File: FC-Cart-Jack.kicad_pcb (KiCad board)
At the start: 2 copper layers, 98 x 56.8 mm, 6 parts, among them J1 ToCartridge, J2 ToConsole, J3 AudioJack3_SwitchTR, U1 LM321

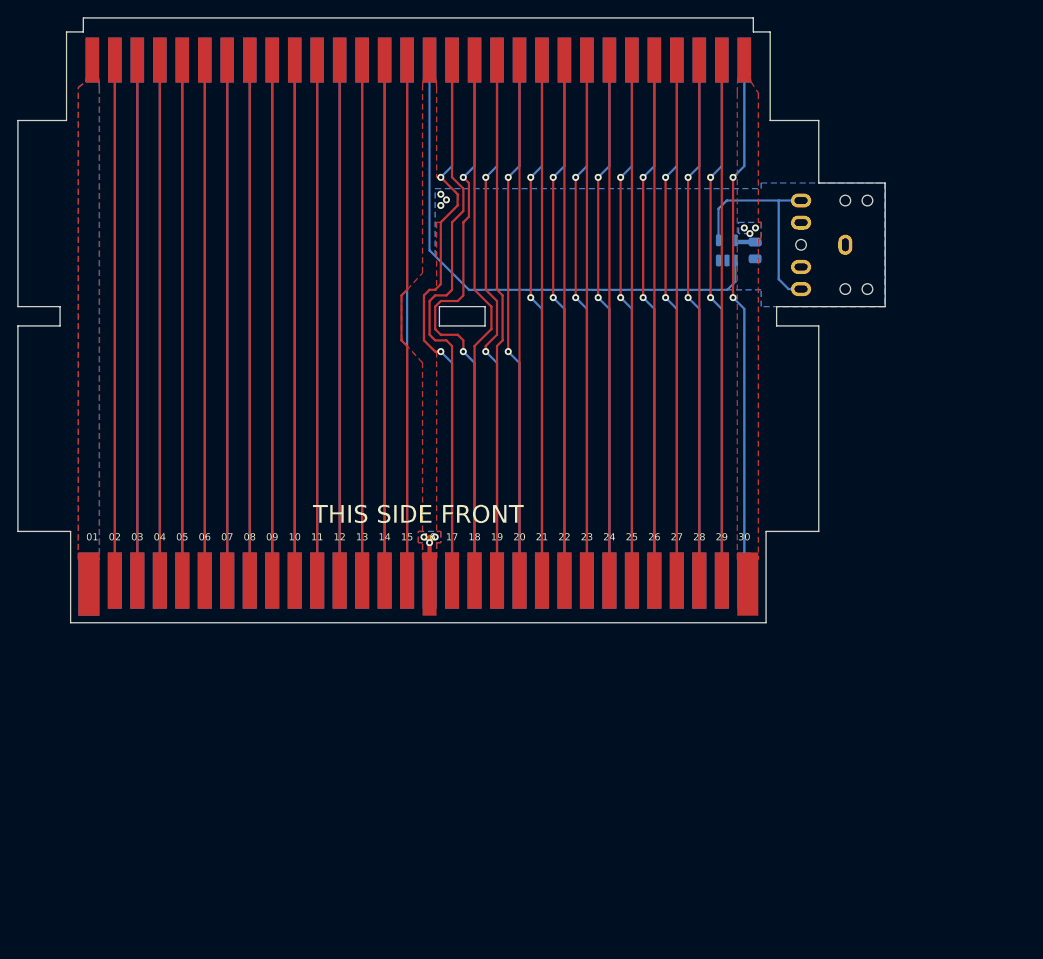
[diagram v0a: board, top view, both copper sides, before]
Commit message: Add silkscreen art
Dagga illustration by @Lockster-Inc
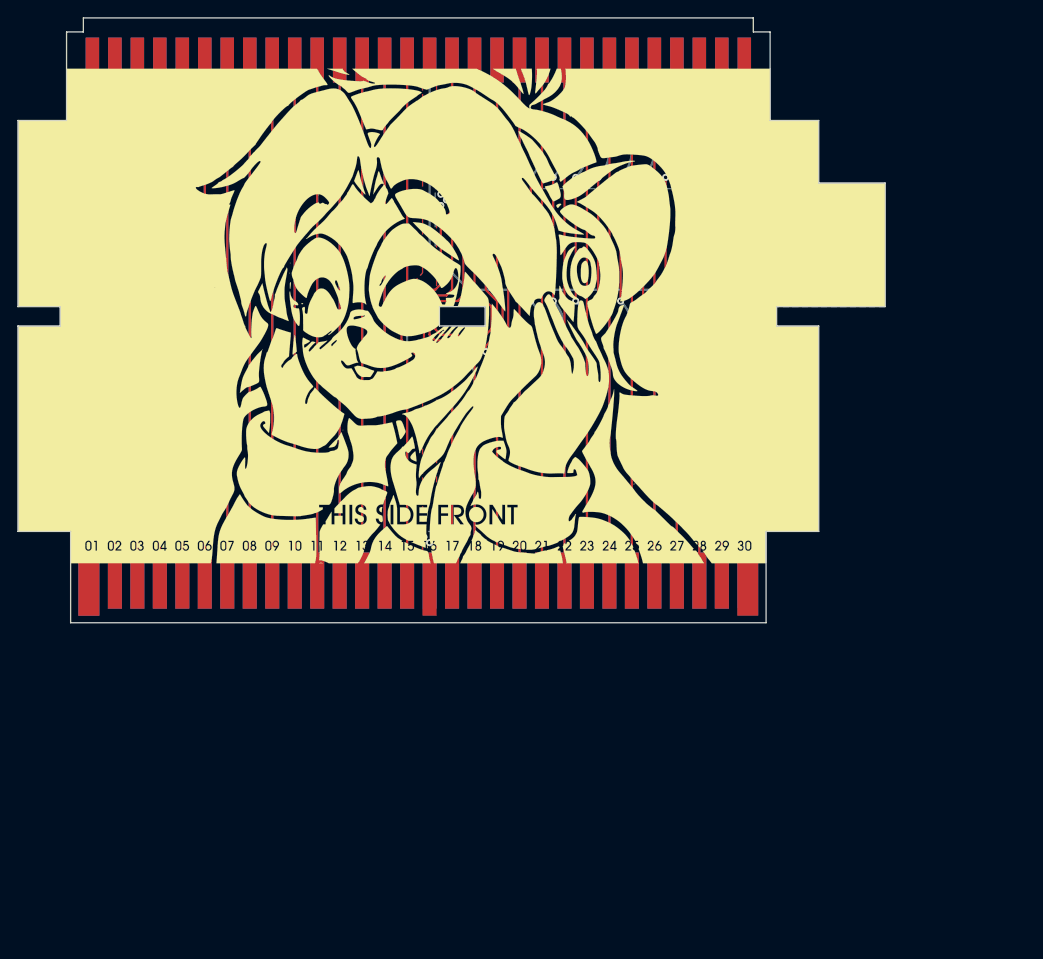
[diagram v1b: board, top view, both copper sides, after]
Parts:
- removed REF**: OSHW-Logo_7.5x8mm_Copper, Symbol:OSHW-Logo_7.5x8mm_Copper
- added Ref**: Val**, custom footprints:art front, F.Cu at (109.2, 67.3)
- added Ref**: Val**, custom footprints:oshw-logo, B.Cu at (137.8, 58.4)
- added Ref**: Val**, custom footprints:art back, B.Cu at (109.2, 67.3)
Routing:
- net /AUD_Output: track 25.2 -> 31.1 mm, vias 0 -> 1
- net GND: track 5.32 -> 0.00 mm
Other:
- board text removed: "01"
- board text removed: "02"
- board text removed: "03"
- board text removed: "04"
- board text removed: "05"
- board text removed: "06"
- board text removed: "07"
- board text removed: "08"
- board text removed: "09"
- board text removed: "10"
- board text removed: "11"
- board text removed: "12"
- board text removed: "13"
- board text removed: "14"
- board text removed: "15"
- board text removed: "16"
- board text removed: "17"
- board text removed: "18"
- board text removed: "19"
- board text removed: "20"
- board text removed: "21"
- board text removed: "22"
- board text removed: "23"
- board text removed: "24"
- board text removed: "25"
- board text removed: "26"
- board text removed: "27"
- board text removed: "28"
- board text removed: "29"
- board text removed: "30"
- board text removed: "31"
- board text removed: "32"
- board text removed: "33"
- board text removed: "34"
- board text removed: "35"
- board text removed: "36"
- board text removed: "37"
- board text removed: "38"
- board text removed: "39"
- board text removed: "40"
- board text removed: "41"
- board text removed: "42"
- board text removed: "43"
- board text removed: "44"
- board text removed: "45"
- board text removed: "46"
- board text removed: "47"
- board text removed: "48"
- board text removed: "49"
- board text removed: "50"
- board text removed: "51"
- board text removed: "52"
- board text removed: "53"
- board text removed: "54"
- board text removed: "55"
- board text removed: "56"
- board text removed: "57"
- board text removed: "58"
- board text removed: "59"
- board text removed: "60"
- board text removed: "FC Cartridge Audio Jack Persune © 2021 Rev. 0.0.1"
- board text removed: "THIS SIDE BACK"
- board text removed: "THIS SIDE FRONT"

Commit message: Update to KiCad 6.0
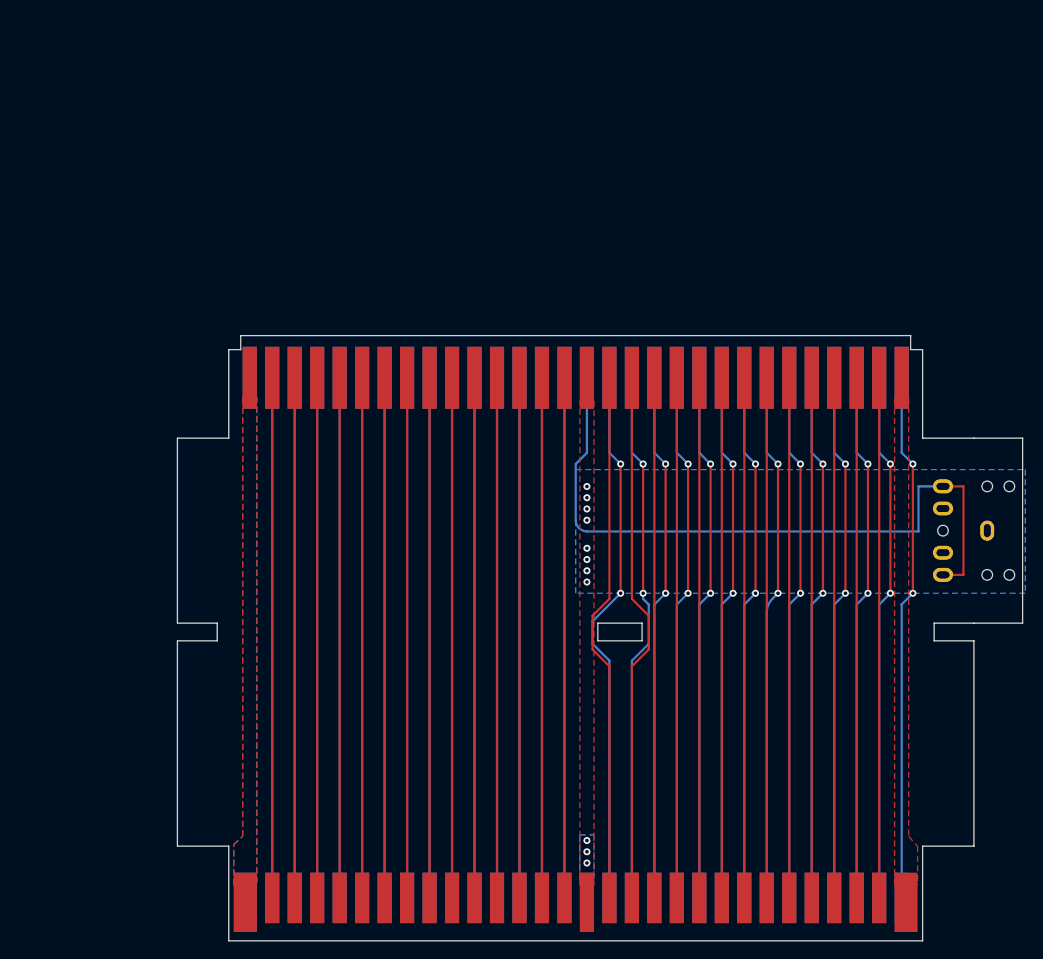
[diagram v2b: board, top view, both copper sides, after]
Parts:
- removed C1: 100nF, Capacitor_SMD:C_0805_2012Metric
- removed Ref**: Val**, custom footprints:art front
- removed Ref**: Val**, custom footprints:oshw-logo
- removed Ref**: Val**, custom footprints:art back
- removed U1: LM321, Package_TO_SOT_SMD:SOT-23-5
- J1: footprint custom footprints:card edge -> FC-Cart-Jack:card edge
- J2: footprint custom footprints:HVC-TGROM-01 -> FC-Cart-Jack:HVC-TGROM-01
- J3: value AudioJack3_SwitchTR -> ~; footprint custom footprints:SJ1-3524NG -> FC-Cart-Jack:SJ1-3524NG
- moved J1 40.1 mm to (127.0, 80.9)
- moved J2 39.8 mm to (127.0, 127.0)
- moved J3 36.1 mm to (178.0, 91.3)
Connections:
- J1 pad 46: /AUD_FromCart -> /AUD_Output
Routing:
- net /AUD_FromCart: track 60.8 -> 0.00 mm
- net /AUD_Output: track 31.1 -> 78.5 mm, vias 1 -> 0
- net /CIRAM_~{CE}: track 64.9 -> 60.4 mm
- net /PPU_~{RD}: track 63.5 -> 60.4 mm
- net VCC: track 2.25 -> 0.00 mm, vias 3 -> 0
- net /PPU_~{WR}: track 63.4 -> 61.4 mm
- net /PPU_D7: track 58.9 -> 59.8 mm
- net /PPU_D6: track 58.9 -> 59.8 mm
- net /PPU_~{A13}: track 60.6 -> 59.8 mm
- net /~{IRQ}: track 59.4 -> 58.8 mm
- net /PPU_A6: track 59.4 -> 58.8 mm
- net GND: vias 6 -> 11
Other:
- board size 98 x 56.8 mm -> 90 x 56.8 mm

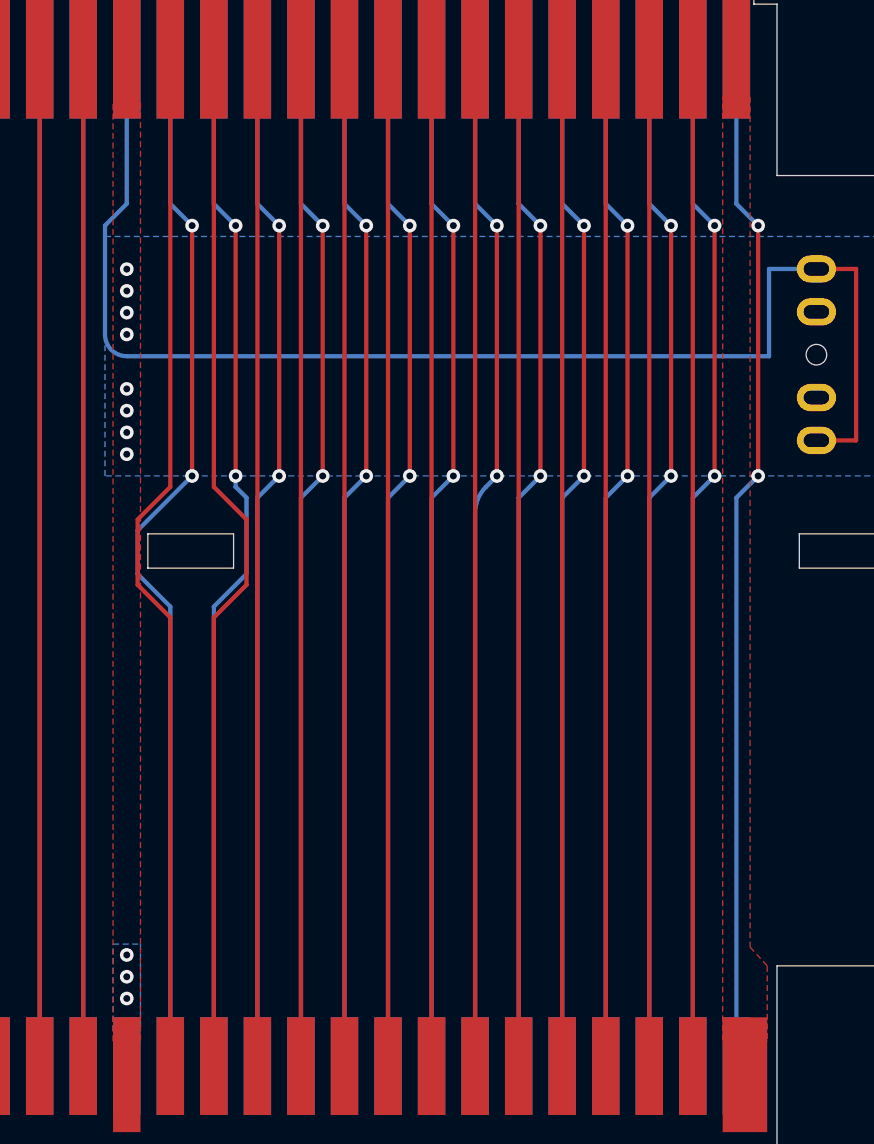
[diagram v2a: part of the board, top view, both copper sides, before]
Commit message: Leave audio out floating
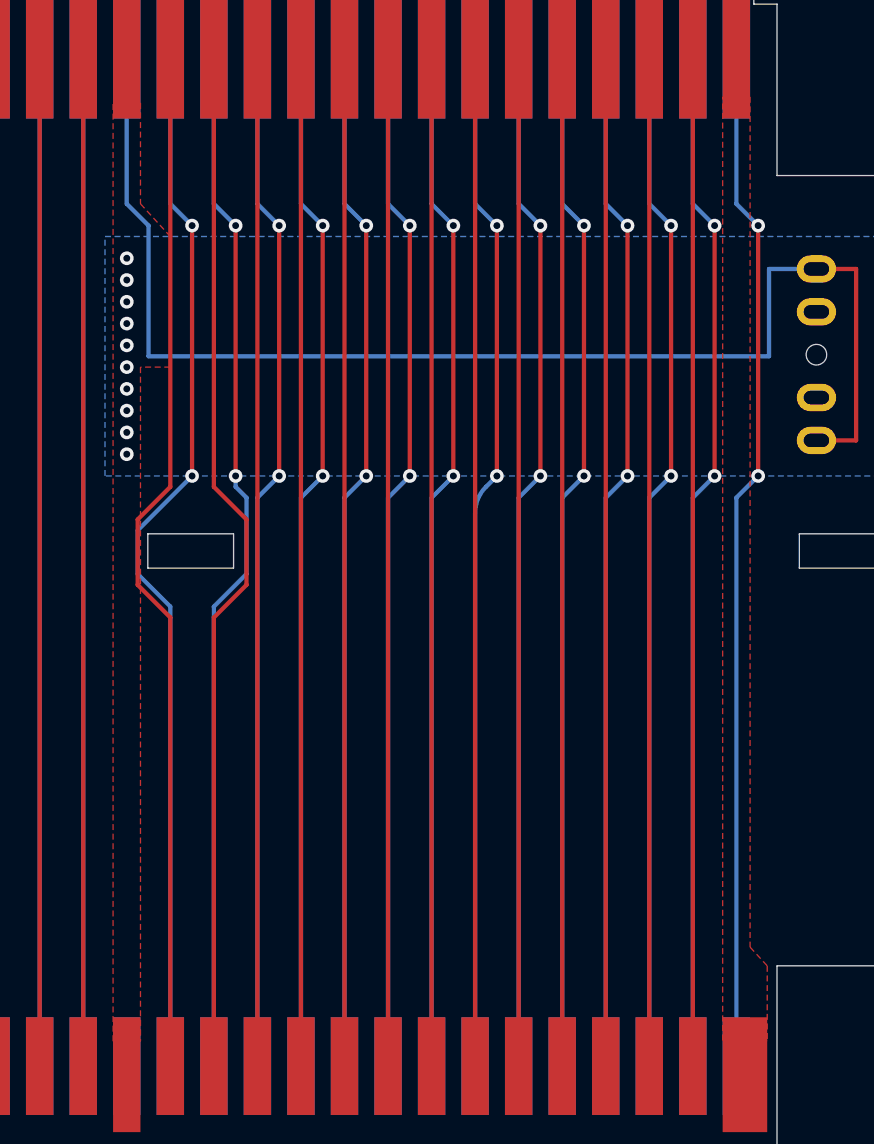
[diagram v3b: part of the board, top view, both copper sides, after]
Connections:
- net /AUD_From2A03 renamed /AUD_2A03
- J2 pad 46: GND -> unconnected-(J2-Pad46)
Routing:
- net /AUD_Output: track 78.5 -> 76.6 mm
- net GND: vias 11 -> 10
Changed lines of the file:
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@@
   (title_block
     (title "FC Cartridge Audio Jack")
-    (date "2022-04-28")
-    (rev "0.0.3")
+    (date "2022-11-14")
+    (rev "0.0.5")
     (company "Persune")
   )
@@
   (net 39 "/CPU_D0")
   (net 40 "/~{ROMSEL}")
-  (net 41 "/AUD_From2A03")
+  (net 41 "/AUD_2A03")
   (net 42 "/PPU_~{WR}")
   (net 43 "/CIRAM_~{CE}")
@@
   (net 57 "GND")
   (net 58 "VCC")
+  (net 59 "unconnected-(J2-Pad46)")
   (footprint "FC-Cart-Jack:card edge" (layer "F.Cu")
     (at 127 80.9)
@@
       (net 40 "/~{ROMSEL}") (pinfunction "Pin_44") (pintype "passive"))
     (pad "45" smd rect (at -1.27 -6.825) (size 1.6 7) (layers "B.Cu" "B.Mask")
-      (net 41 "/AUD_From2A03") (pinfunction "Pin_45") (pintype "passive"))
+      (net 41 "/AUD_2A03") (pinfunction "Pin_45") (pintype "passive"))
     (pad "46" smd rect (at 1.27 -6.825) (size 1.6 7) (layers "B.Cu" "B.Mask")
       (net 56 "/AUD_Output") (pinfunction "Pin_46") (pintype "passive"))
@@
       (net 40 "/~{ROMSEL}") (pinfunction "Pin_44") (pintype "passive"))
     (pad "45" connect rect (at -1.27 5.85) (size 1.6 5.7) (layers "B.Cu")
-      (net 41 "/AUD_From2A03") (pinfunction "Pin_45") (pintype "passive"))
+      (net 41 "/AUD_2A03") (pinfunction "Pin_45") (pintype "passive"))
     (pad "46" connect rect (at 1.27 5.85) (size 1.6 5.7) (layers "B.Cu")
-      (net 57 "GND") (pinfunction "Pin_46") (pintype "passive"))
+      (net 59 "unconnected-(J2-Pad46)") (pinfunction "Pin_46") (pintype "passive+no_connect"))
     (pad "47" connect rect (at 3.81 5.85) (size 1.6 5.7) (layers "B.Cu")
       (net 42 "/PPU_~{WR}") (pinfunction "Pin_47") (pintype "passive"))
@@
   (segment (start 170.815 96.35) (end 168.5 96.35) (width 0.25) (layer "F.Cu") (net 56))
   (segment (start 168.5 86.35) (end 170.815 86.35) (width 0.25) (layer "F.Cu") (net 56))
+  (segment (start 129.54 91.44) (end 129.54 83.82) (width 0.25) (layer "B.Cu") (net 56))
   (segment (start 165.735 86.35) (end 165.735 91.44) (width 0.25) (layer "B.Cu") (net 56))
-  (segment (start 165.735 91.44) (end 128.27 91.44) (width 0.25) (layer "B.Cu") (net 56))
-  (segment (start 127 83.82) (end 128.27 82.55) (width 0.25) (layer "B.Cu") (net 56))
   (segment (start 128.27 82.55) (end 128.27 74.075) (width 0.25) (layer "B.Cu") (net 56))
-  (segment (start 127 90.17) (end 127 83.82) (width 0.25) (layer "B.Cu") (net 56))
   (segment (start 168.5 86.35) (end 165.735 86.35) (width 0.25) (layer "B.Cu") (net 56))
-  (arc (start 127 90.17) (mid 127.371975 91.068025) (end 128.27 91.44) (width 0.25) (layer "B.Cu") (net 56))
-  (via (at 128.27 127.635) (size 0.8) (drill 0.4) (layers "F.Cu" "B.Cu") (free) (net 57))
-  (via (at 128.27 87.63) (size 0.8) (drill 0.4) (layers "F.Cu" "B.Cu") (free) (net 57))
+  (segment (start 165.735 91.44) (end 129.54 91.44) (width 0.25) (layer "B.Cu") (net 56))
+  (segment (start 129.54 83.82) (end 128.27 82.55) (width 0.25) (layer "B.Cu") (net 56))
+  (via (at 128.27 86.995) (size 0.8) (drill 0.4) (layers "F.Cu" "B.Cu") (free) (net 57))
+  (via (at 128.27 88.265) (size 0.8) (drill 0.4) (layers "F.Cu" "B.Cu") (free) (net 57))
+  (via (at 128.27 90.805) (size 0.8) (drill 0.4) (layers "F.Cu" "B.Cu") (free) (net 57))
   (via (at 128.27 94.615) (size 0.8) (drill 0.4) (layers "F.Cu" "B.Cu") (free) (net 57))
-  (via (at 128.27 126.365) (size 0.8) (drill 0.4) (layers "F.Cu" "B.Cu") (free) (net 57))
-  (via (at 128.27 88.9) (size 0.8) (drill 0.4) (layers "F.Cu" "B.Cu") (free) (net 57))
-  (via (at 128.27 128.905) (size 0.8) (drill 0.4) (layers "F.Cu" "B.Cu") (free) (net 57))
-  (via (at 128.27 90.17) (size 0.8) (drill 0.4) (layers "F.Cu" "B.Cu") (free) (net 57))
+  (via (at 128.27 85.725) (size 0.8) (drill 0.4) (layers "F.Cu" "B.Cu") (free) (net 57))
+  (via (at 128.27 89.535) (size 0.8) (drill 0.4) (layers "F.Cu" "B.Cu") (free) (net 57))
   (via (at 128.27 93.345) (size 0.8) (drill 0.4) (layers "F.Cu" "B.Cu") (free) (net 57))
-  (via (at 128.27 86.36) (size 0.8) (drill 0.4) (layers "F.Cu" "B.Cu") (free) (net 57))
+  (via (at 128.27 92.075) (size 0.8) (drill 0.4) (layers "F.Cu" "B.Cu") (free) (net 57))
   (via (at 128.27 97.155) (size 0.8) (drill 0.4) (layers "F.Cu" "B.Cu") (free) (net 57))
   (via (at 128.27 95.885) (size 0.8) (drill 0.4) (layers "F.Cu" "B.Cu") (free) (net 57))
@@
     (polygon
       (pts
+        (xy 129.07 82.55)
+        (xy 130.81 84.455)
+        (xy 130.81 92.075)
+        (xy 129.07 92.075)
         (xy 129.07 131.4)
         (xy 127.47 131.4)
@@
       )
     )
-  )
-  (zone (net 57) (net_name "GND") (layer "B.Cu") (hatch edge 0.508)
-    (priority 2)
-    (connect_pads yes (clearance 0.254))
-    (min_thickness 0.254) (filled_areas_thickness no)
-    (fill yes (thermal_gap 0.508) (thermal_bridge_width 0.508) (smoothing fillet) (radius 2))
-    (polygon
-      (pts
-        (xy 129.07 130.81)
-        (xy 127.47 130.81)
-        (xy 127.47 125.73)
-        (xy 129.07 125.73)
-      )
-    )
